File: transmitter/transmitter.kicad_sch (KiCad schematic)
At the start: 1 part, among them U1 NRF24L01_Breakout

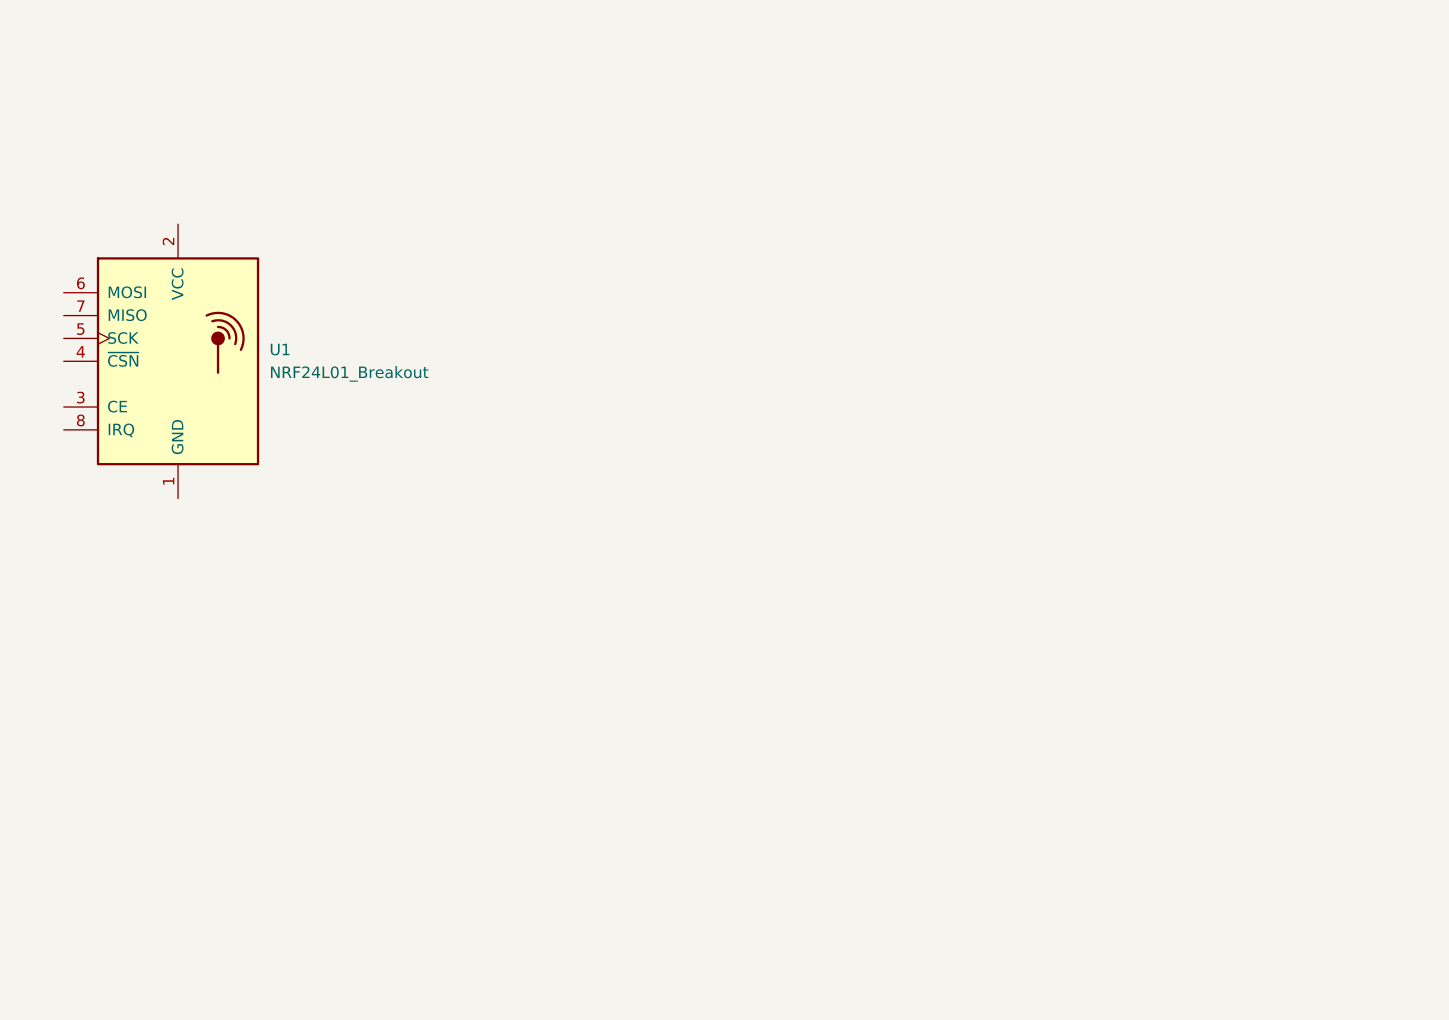
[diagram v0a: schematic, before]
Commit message: Added transmitter schematic, and fixed readme
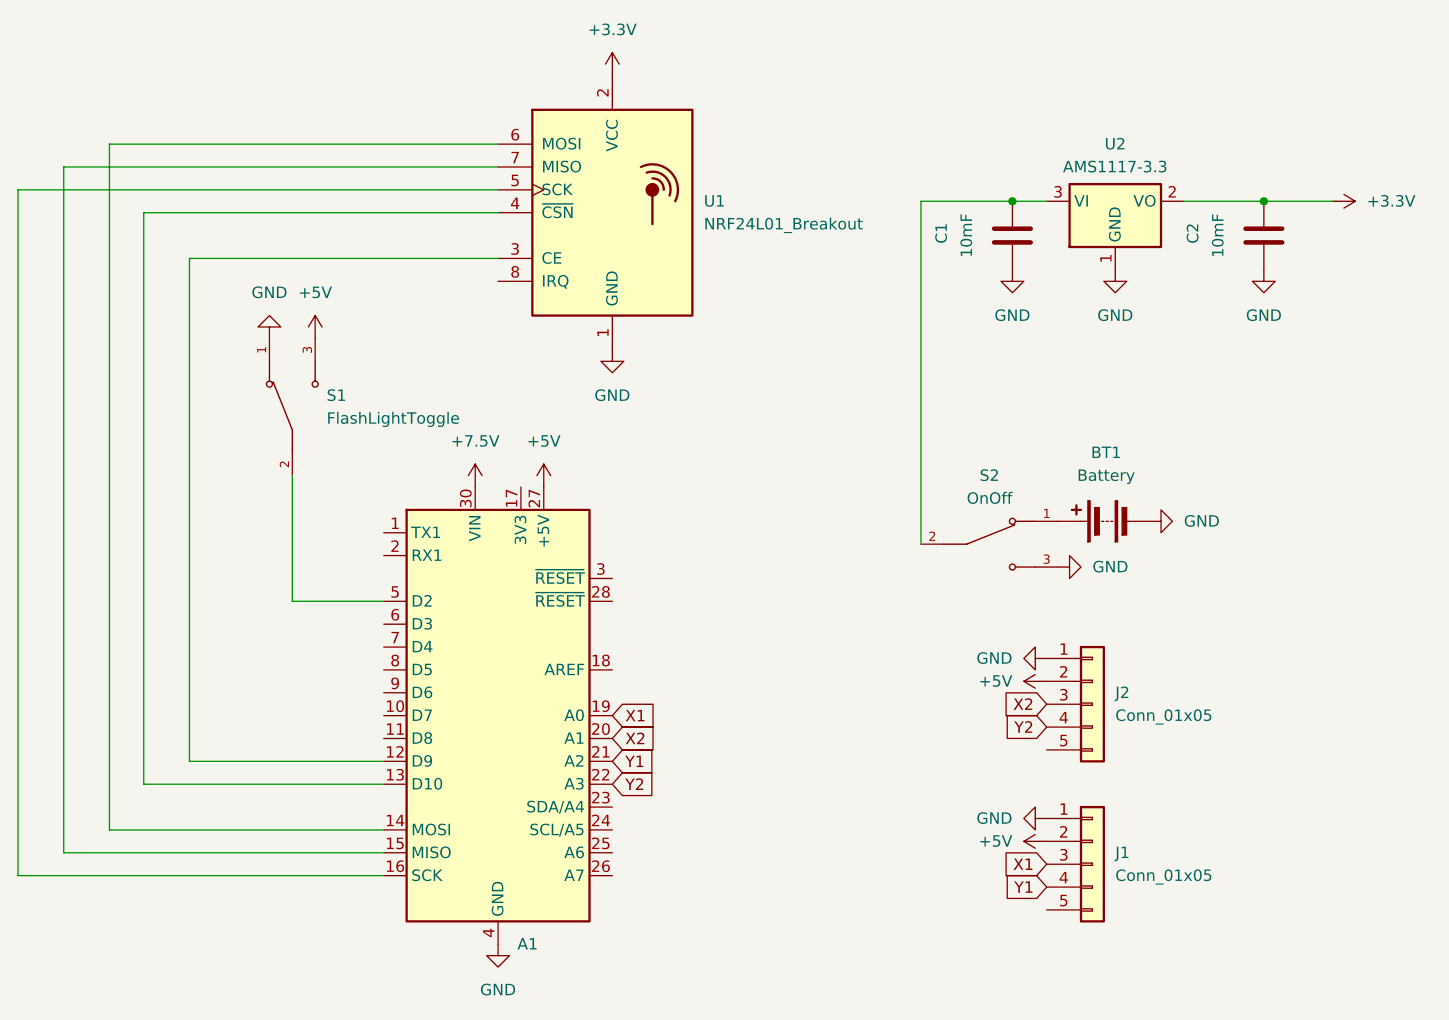
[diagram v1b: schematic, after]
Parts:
- added A1: Arduino_Nano_Every, Module:Arduino_Nano, symbol MCU_Module:Arduino_Nano_Every
- added BT1: Battery, Connector_JST:JST_XH_B3B-XH-A_1x03_P2.50mm_Vertical, symbol Device:Battery
- added C1, C2: 10mF, Capacitor_THT:CP_Radial_D8.0mm_P5.00mm, symbol Device:C
- added J1, J2: Conn_01x05, Connector_PinHeader_2.54mm:PinHeader_1x05_P2.54mm_Vertical, symbol Connector_Generic:Conn_01x05
- added S1: FlashLightToggle, 100SP1T1B4M2QE:SW_100SP1T1B4M2QE, symbol ToggleSwitch:100SP1T1B4M2QE
- added S2: OnOff, 100SP1T1B4M2QE:SW_100SP1T1B4M2QE, symbol ToggleSwitch:100SP1T1B4M2QE
- added U2: AMS1117-3.3, Package_TO_SOT_SMD:SOT-223-3_TabPin2, symbol Regulator_Linear:AMS1117-3.3
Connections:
- net GND: now reaches U1.1 (GND)
- net GND: now also A1.29 (GND), A1.4 (GND), BT1.2 (-), C1.1, C2.1, J1.1 (Pin_1), J2.1 (Pin_1), S1.1, S2.3, U2.1 (GND)
- net +3.3V: now reaches U1.2 (VCC)
- net +3.3V: now also C2.2, U2.2 (VO)
- net at U1.3 (CE): now also A1.12 (D9)
- net at U1.4 (~{CSN}): now also A1.13 (D10)
- net at U1.5 (SCK): now also A1.16 (SCK)
- net at U1.6 (MOSI): now also A1.14 (MOSI)
- net at U1.7 (MISO): now also A1.15 (MISO)
- new net: A1.5 (D2), S1.2
- new net: C1.2, S2.2, U2.3 (VI)
- new net: BT1.1 (+), S2.1
- new net +5V: A1.27 (+5V), J1.2 (Pin_2), J2.2 (Pin_2), S1.3
- new net +7.5V: A1.30 (VIN)
- new net X1: A1.19 (A0), J1.3 (Pin_3)
- new net X2: A1.20 (A1), J2.3 (Pin_3)
- new net Y1: A1.21 (A2), J1.4 (Pin_4)
- new net Y2: A1.22 (A3), J2.4 (Pin_4)
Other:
- moved on the sheet: U1

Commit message: Completed transmitter PCB and rough BOM, updated journal
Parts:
- BT1: footprint Connector_JST:JST_XH_B3B-XH-A_1x03_P2.50mm_Vertical -> Connector_PinHeader_2.54mm:PinHeader_1x02_P2.54mm_Vertical
- S1, S2: footprint 100SP1T1B4M2QE:SW_100SP1T1B4M2QE -> Button_Switch_THT:SW_Slide_SPDT_Straight_CK_OS102011MS2Q
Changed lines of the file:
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@@
 			)
 		)
-		(property "Footprint" "100SP1T1B4M2QE:SW_100SP1T1B4M2QE"
+		(property "Footprint" "Button_Switch_THT:SW_Slide_SPDT_Straight_CK_OS102011MS2Q"
 			(at 107.95 76.2 0)
 			(effects
@@
 			)
 		)
-		(property "Footprint" "100SP1T1B4M2QE:SW_100SP1T1B4M2QE"
+		(property "Footprint" "Button_Switch_THT:SW_Slide_SPDT_Straight_CK_OS102011MS2Q"
 			(at 185.42 91.44 0)
 			(effects
@@
 			)
 		)
-		(property "Footprint" "Connector_JST:JST_XH_B3B-XH-A_1x03_P2.50mm_Vertical"
+		(property "Footprint" "Connector_PinHeader_2.54mm:PinHeader_1x02_P2.54mm_Vertical"
 			(at 196.596 88.9 90)
 			(effects
